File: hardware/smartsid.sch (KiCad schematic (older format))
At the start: 46 parts, among them P1 INPUT, P2 CONTROL, P3 POT2, P4 SOCKET, P5 OUTPUT, U1 GAL16V8, U2 SID2, U3 7812, U4 7809, U5 SID1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

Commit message: Hardware: Added some proper pinheaders, new routing, added more docs
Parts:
- JP1, JP2, JP3, JP4, JP5, JP6, JP7, P3, P5: footprint Pin_Headers:Pin_Header_Straight_1x03 -> Pinheaders:Pin_Header_Straight_1x03
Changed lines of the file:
@@
 F 0 "P3" H 1250 3000 50  0000 C CNN
 F 1 "POT2" V 1350 2800 50  0000 C CNN
-F 2 "Pin_Headers:Pin_Header_Straight_1x03" H 1250 2800 60  0001 C CNN
+F 2 "Pinheaders:Pin_Header_Straight_1x03" H 1250 2800 60  0001 C CNN
 F 3 "" H 1250 2800 60  0000 C CNN
 	1    1250 2800
@@
 F 0 "JP2" H 4350 2550 50  0000 L CNN
 F 1 "S2CAP2" H 4300 2750 50  0000 C BNN
-F 2 "Pin_Headers:Pin_Header_Straight_1x03" H 4300 2650 60  0001 C CNN
+F 2 "Pinheaders:Pin_Header_Straight_1x03" H 4300 2650 60  0001 C CNN
 F 3 "" H 4300 2650 60  0000 C CNN
 	1    4300 2650
@@
 F 0 "JP3" H 4350 3200 50  0000 L CNN
 F 1 "S2CAP1" H 4300 3400 50  0000 C BNN
-F 2 "Pin_Headers:Pin_Header_Straight_1x03" H 4300 3300 60  0001 C CNN
+F 2 "Pinheaders:Pin_Header_Straight_1x03" H 4300 3300 60  0001 C CNN
 F 3 "" H 4300 3300 60  0000 C CNN
 	1    4300 3300
@@
 F 0 "JP6" H 7350 2600 50  0000 L CNN
 F 1 "S1CAP2" H 7300 2800 50  0000 C BNN
-F 2 "Pin_Headers:Pin_Header_Straight_1x03" H 7300 2700 60  0001 C CNN
+F 2 "Pinheaders:Pin_Header_Straight_1x03" H 7300 2700 60  0001 C CNN
 F 3 "" H 7300 2700 60  0000 C CNN
 	1    7300 2700
@@
 F 0 "JP7" H 7350 3250 50  0000 L CNN
 F 1 "S1CAP1" H 7300 3450 50  0000 C BNN
-F 2 "Pin_Headers:Pin_Header_Straight_1x03" H 7300 3350 60  0001 C CNN
+F 2 "Pinheaders:Pin_Header_Straight_1x03" H 7300 3350 60  0001 C CNN
 F 3 "" H 7300 3350 60  0000 C CNN
 	1    7300 3350
@@
 F 0 "JP1" H 4200 1250 50  0000 L CNN
 F 1 "SUPPLY2" H 4150 1450 50  0000 C BNN
-F 2 "Pin_Headers:Pin_Header_Straight_1x03" H 4150 1350 60  0001 C CNN
+F 2 "Pinheaders:Pin_Header_Straight_1x03" H 4150 1350 60  0001 C CNN
 F 3 "" H 4150 1350 60  0000 C CNN
 	1    4150 1350
@@
 F 0 "JP5" H 7200 1300 50  0000 L CNN
 F 1 "SUPPLY1" H 7150 1500 50  0000 C BNN
-F 2 "Pin_Headers:Pin_Header_Straight_1x03" H 7150 1400 60  0001 C CNN
+F 2 "Pinheaders:Pin_Header_Straight_1x03" H 7150 1400 60  0001 C CNN
 F 3 "" H 7150 1400 60  0000 C CNN
 	1    7150 1400
@@
 F 0 "JP4" H 4200 6850 50  0000 L CNN
 F 1 "BOARD" H 4150 7050 50  0000 C BNN
-F 2 "Pin_Headers:Pin_Header_Straight_1x03" H 4150 6950 60  0001 C CNN
+F 2 "Pinheaders:Pin_Header_Straight_1x03" H 4150 6950 60  0001 C CNN
 F 3 "" H 4150 6950 60  0000 C CNN
 	1    4150 6950
@@
 F 0 "P5" H 850 3650 50  0000 C CNN
 F 1 "OUTPUT" V 950 3450 50  0000 C CNN
-F 2 "Pin_Headers:Pin_Header_Straight_1x03" H 850 3450 60  0001 C CNN
+F 2 "Pinheaders:Pin_Header_Straight_1x03" H 850 3450 60  0001 C CNN
 F 3 "" H 850 3450 60  0000 C CNN
 	1    850  3450

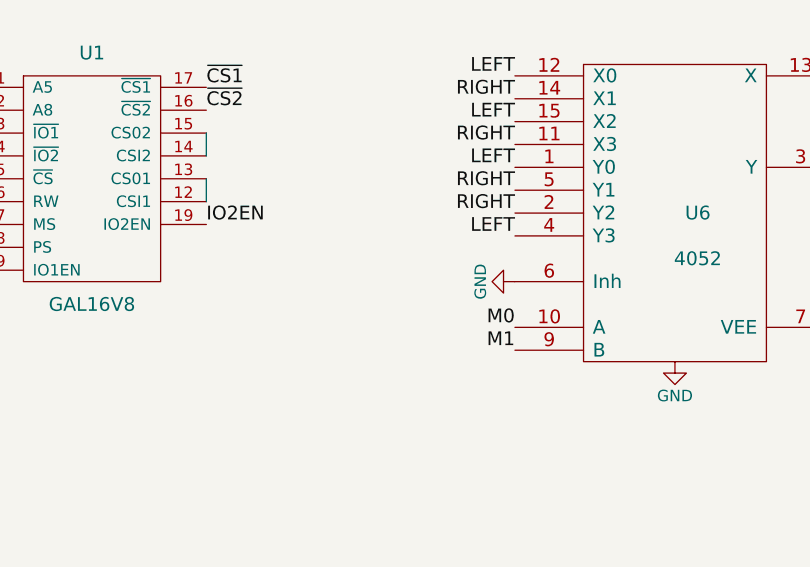
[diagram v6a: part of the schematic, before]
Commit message: Hardware: Added pullups for M0 and M1, rerouted
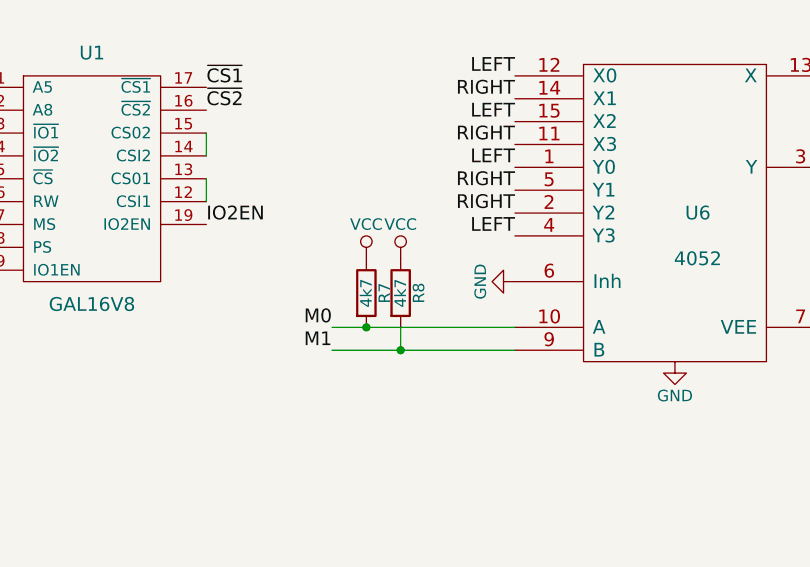
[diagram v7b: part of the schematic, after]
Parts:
- added R7, R8: 4k7, Discret:R3, symbol R
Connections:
- net M0: now also R7.2
- net M1: now also R8.2
- net VCC: now also R7.1, R8.1
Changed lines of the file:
@@
 encoding utf-8
 Sheet 1 1
-Title ""
-Date ""
-Rev ""
-Comp ""
-Comment1 ""
+Title "SmartSID - C64 stereo SID addon board"
+Date "2016-03-09"
+Rev "1"
+Comp "Henning Bekel"
+Comment1 "www.henning-bekel.de/smartsid"
 Comment2 ""
 Comment3 ""
@@
 	0    1    1    0
 $EndComp
-Text Label 4700 5450 2    60   ~ 0
+Text Label 3900 5450 2    60   ~ 0
 M0
-Text Label 4700 5550 2    60   ~ 0
+Text Label 3900 5550 2    60   ~ 0
 M1
 $Comp
@@
 Text Label 3850 6950 0    60   ~ 0
 PWR
+$Comp
+L R R7
+U 1 1 56E0803A
+P 4050 5300
+F 0 "R7" V 4130 5300 50  0000 C CNN
+F 1 "4k7" V 4050 5300 50  0000 C CNN
+F 2 "Discret:R3" V 3980 5300 30  0001 C CNN
+F 3 "" H 4050 5300 30  0000 C CNN
+	1    4050 5300
+	1    0    0    -1
+$EndComp
+$Comp
+L R R8
+U 1 1 56E0814A
+P 4200 5300
+F 0 "R8" V 4280 5300 50  0000 C CNN
+F 1 "4k7" V 4200 5300 50  0000 C CNN
+F 2 "Discret:R3" V 4130 5300 30  0001 C CNN
+F 3 "" H 4200 5300 30  0000 C CNN
+	1    4200 5300
+	1    0    0    -1
+$EndComp
+Wire Wire Line
+	3900 5450 4700 5450
+Connection ~ 4050 5450
+Wire Wire Line
+	3900 5550 4700 5550
+Connection ~ 4200 5550
+$Comp
+L VCC #PWR029
+U 1 1 56E083EC
+P 4050 5150
+F 0 "#PWR029" H 4050 5000 50  0001 C CNN
+F 1 "VCC" H 4050 5300 50  0000 C CNN
+F 2 "" H 4050 5150 60  0000 C CNN
+F 3 "" H 4050 5150 60  0000 C CNN
+	1    4050 5150
+	1    0    0    -1
+$EndComp
+$Comp
+L VCC #PWR030
+U 1 1 56E08491
+P 4200 5150
+F 0 "#PWR030" H 4200 5000 50  0001 C CNN
+F 1 "VCC" H 4200 5300 50  0000 C CNN
+F 2 "" H 4200 5150 60  0000 C CNN
+F 3 "" H 4200 5150 60  0000 C CNN
+	1    4200 5150
+	1    0    0    -1
+$EndComp
+Wire Wire Line
+	4200 5550 4200 5450
 $EndSCHEMATC

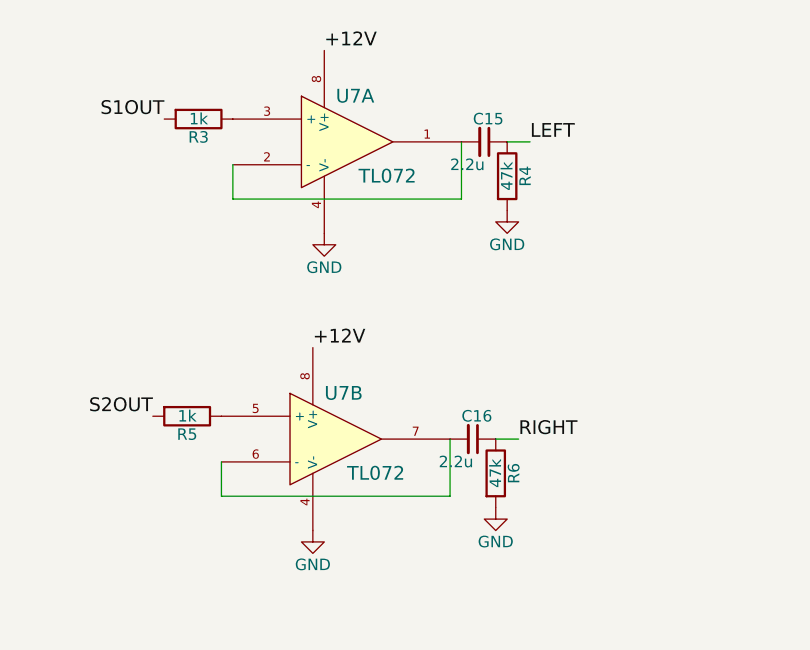
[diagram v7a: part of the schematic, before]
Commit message: Hardware: Improved routing, changed opamp from TL072 to OPA132
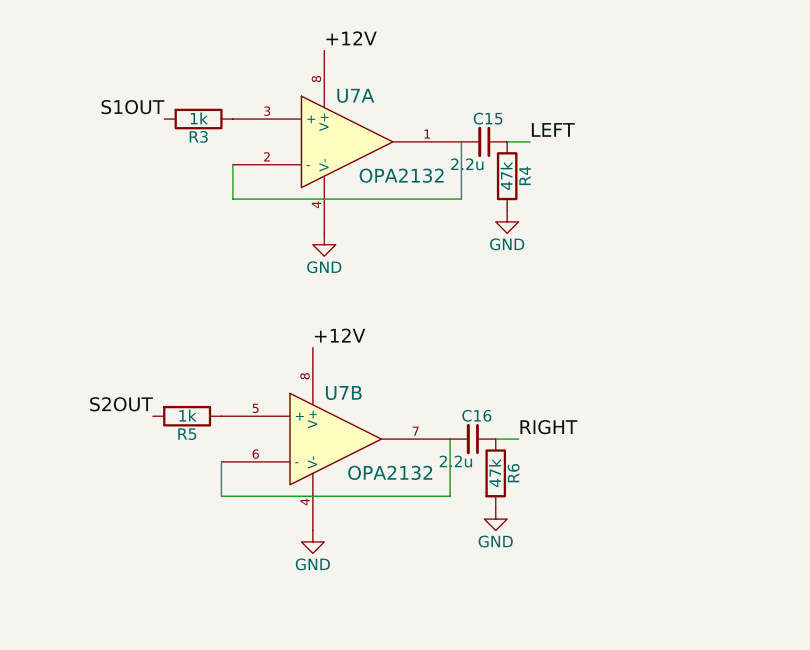
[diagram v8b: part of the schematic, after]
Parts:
- U7: value TL072 -> OPA2132
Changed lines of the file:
@@
 P 9100 5600
 F 0 "U7" H 9050 5800 60  0000 L CNN
-F 1 "TL072" H 9150 5450 60  0000 L CNN
+F 1 "OPA2132" H 9150 5450 60  0000 L CNN
 F 2 "Housings_DIP:DIP-8_W7.62mm" H 9100 5600 60  0001 C CNN
 F 3 "" H 9100 5600 60  0000 C CNN
@@
 P 9150 4300
 F 0 "U7" H 9100 4500 60  0000 L CNN
-F 1 "TL072" H 9200 4150 60  0000 L CNN
+F 1 "OPA2132" H 9200 4150 60  0000 L CNN
 F 2 "Housings_DIP:DIP-8_W7.62mm" H 9150 4300 60  0001 C CNN
 F 3 "" H 9150 4300 60  0000 C CNN
